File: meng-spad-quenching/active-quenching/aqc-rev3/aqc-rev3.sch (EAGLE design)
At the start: 274 parts, among them IC1 TPS7A4901, IC10 TPS7A3001, IC11 LT1534-1, IC12 74AHC1G04DCK, IC13 TLV271DBV, IC14 NC7WZ16P6X, IC15 LTC1711, IC16 HFA3134, IC17 HFA3135, IC18 USBLC6-2SC6Y, IC19 HFA3135, IC2 TPS7A4901, IC20 HFA3134, IC21 STM32F411RE, IC22 MAX572X, IC23 HFA3134, IC24 LM1117, IC25 HFA3134, IC26 THAT320, IC27 74AHC1G14DCK, IC28 NL17SZ125, IC29 TLV272DGK, IC3 LT1534-1, IC30 74AHC1G32DCK, IC31 74AHC1G08DCK, IC4 TLV272DGK, IC5 ADCMP582, IC6 DS1100LU-20+, IC7 HFA3134, IC8 NC7SV74K8X, IC9 HFA3134, M2 BSS806N, M3 BSS806N, Q6 IRLML6402TRPBF, SW1 MCU_RST, T1 MMBTH10, U1 MCP4725, U2 SN65EPT22DGK, U3 SN65EPT21DGK, X1 CONN_PULLDN_SENSE, X2 CONN_FORCE_QUENCH, X3 KEYSTONE-7774, X4 CONN_SPAD, X5 CONN_PHOTON_COUNTER, X6 KEYSTONE-7774, X7 CONN_SMU, X8 PN61729-S

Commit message: Fixed one-shot error, layout done
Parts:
- removed D7, D8: BAS40, diode:BAS40
- removed D9: (no value), diode:DIODE-SOD523
- removed L11: MI0805J102R-10, meng:INDUCTOR0805
- removed M3: BSS806N, meng:BSS806N
- removed Q6: IRLML6402TRPBF, microbuilder:MOSFET-PWIDE
- removed R77: 22R, resistor:R-EU_R0402
- removed R78: 0R, rcl-modified-footprints:R-EU_R0603
- removed R79: DNP, rcl-modified-footprints:R-EU_R0603
- removed R80: SOT-DIV23LF-03-1001-1001-BB, meng:DIVIDER_SOT23-5
- removed R82: 0R, rcl:R-EU_R0603
- removed R83, R84: 100R, rcl:R-EU_R0603
- removed R85: 470R, resistor:R-EU_R0603
- added C102: 4u7, rcl:C-EUC0603
- added C112, C90: 100n, rcl:C-EUC0603
- added C87: 100n, rcl-modified-footprints:C-EUC0603
- added C88, C89: 100n, rcl-modified-footprints:C-EUC0402
- added D2: CDBA140SL-HF, diode:DIODE-DO214AC
- added D3: TVS, diode:DIODE-SOD523
- added D5: BAS40, diode:BAS40
- added DNP1000: RLE_LOGO, meng:RLE_LOGO
- added IC32: LM1117, meng:LM1117
- added L8: MI0805J102R-10, meng:INDUCTOR0805
- added M1: BSS806N, meng:BSS806N
- added Q1: IRLML6402TRPBF, microbuilder:MOSFET-PWIDE
- added R47, R51: 0R, rcl-modified-footprints:R-EU_R0603
- added R50: 110R, 1%, rcl-modified-footprints:R-EU_R0603
- added R57: 100k, rcl-modified-footprints:R-EU_R0603
- added R60: 470R, resistor:R-EU_R0603
- added R61: 220k, rcl-modified-footprints:R-EU_R0603
- added R62: 100k, resistor:R-EU_R0603
- added R68: SOT-DIV23LF-03-1001-1001-BB, meng:DIVIDER_SOT23-5
- added R69: DNP, rcl-modified-footprints:R-EU_R0603
- added R70: 22R, resistor:R-EU_R0402
- C100: value 100n -> 47p; device rcl-modified-footprints:C-EUC0603 -> rcl:C-EUC0402
- C101, C23, C28, C36, C42, C45, C7, C76, C78: value 10n -> 100n
- C103, C108, C40, C98: device rcl:C-EUC0603 -> rcl-modified-footprints:C-EUC0603
- C104, C21, C27, C29, C43, C5, C80, C83: value 100n -> 10n
- C105, C99: value 4u7 -> 100n
- C107: value 100n -> 4u7; device rcl-modified-footprints:C-EUC0603 -> rcl:C-EUC0603
- C11: value 100n -> 10u; device rcl-modified-footprints:C-EUC0603 -> rcl:C-EUC0805
- C13: value 10u -> 47u, 20V; device rcl:C-EUC0805 -> rcl:CPOL-EUCT7343
- C15: value 47u, 20V -> 4u7; device rcl:CPOL-EUCT7343 -> rcl:C-EUC0805
- C16: value 4u7 -> 100n; device rcl:C-EUC0805 -> rcl-modified-footprints:C-EUC0603
- C17: value 4u7 -> 100n; device rcl-modified-footprints:C-EUC0603 -> rcl:C-EUC0603
- C18: value 100n -> 15n; device rcl-modified-footprints:C-EUC0603 -> rcl:C-EUC0603
- C19: value 10n -> 220p; device rcl-modified-footprints:C-EUC0402 -> rcl:C-EUC0603
- C20: value 10n -> 100n; device rcl-modified-footprints:C-EUC0402 -> rcl-modified-footprints:C-EUC0603
- C22: value 10n -> 4u7; device rcl-modified-footprints:C-EUC0402 -> rcl-modified-footprints:C-EUC0603
- C24, C84: value 100n -> 10n; device rcl:C-EUC0603 -> rcl-modified-footprints:C-EUC0402
- C25: value 15n -> 47u, 20V; device rcl:C-EUC0603 -> rcl:CPOL-EUCT7343
- C26: value 220p -> 47u, 20V; device rcl:C-EUC0603 -> rcl:CPOL-EUCT7343
- C30: value 47u, 20V -> 10n; device rcl:CPOL-EUCT7343 -> rcl:C-EUC0603
- C31: value 47u, 20V -> 1300p; device rcl:CPOL-EUCT7343 -> rcl:C-EUC0603
- C38: value 100n -> 10u; device rcl-modified-footprints:C-EUC0402 -> rcl:C-EUC0805
- C41: value 1300p -> 68u, 16V; device rcl:C-EUC0603 -> rcl:CPOL-EUCT7343
- C44: value 10u -> 4u7
- C46: value 68u, 16V -> 10n; device rcl:CPOL-EUCT7343 -> rcl-modified-footprints:C-EUC0402
- C50: value 100n -> 100p
- C51: device rcl:C-EUC0402 -> rcl-modified-footprints:C-EUC0603
- C53: value 4u7 -> 10n; device rcl:C-EUC0805 -> rcl-modified-footprints:C-EUC0603
- C54, C62, C77: device rcl:C-EUC0402 -> rcl-modified-footprints:C-EUC0402
- C55: value 10n -> 10u, 10V; device rcl:C-EUC0402 -> rcl:C-EUC0805
- C56: value 100p -> 4u7; device rcl-modified-footprints:C-EUC0402 -> rcl:C-EUC0805
- C57: value 10n -> 100n; device rcl-modified-footprints:C-EUC0603 -> rcl-modified-footprints:C-EUC0402
- C58, C92: device rcl-modified-footprints:C-EUC0603 -> rcl-modified-footprints:C-EUC0402
- C59: device rcl-modified-footprints:C-EUC0603 -> rcl:C-EUC0402
- C60: value 10u, 10V -> 100n; device rcl:C-EUC0805 -> rcl:C-EUC0402
- C61: value 4u7 -> 10n; device rcl:C-EUC0805 -> rcl-modified-footprints:C-EUC0402
- C63: value 100n -> 10n; device rcl:C-EUC0402 -> rcl-modified-footprints:C-EUC0402
- C65, C73: value 100n -> 10n; device rcl-modified-footprints:C-EUC0402 -> rcl:C-EUC0402
- C66: value 100p -> 100n; device rcl-modified-footprints:C-EUC0603 -> rcl:C-EUC0603
- C67: value 100n -> 33n
- C68: value 33n -> DNP
- C69: value DNP -> 100p; device rcl:C-EUC0603 -> rcl-modified-footprints:C-EUC0603
- C71: value 100n -> DNP; device rcl-modified-footprints:C-EUC0603 -> rcl-modified-footprints:C-EUC0402
- C72: value 10n -> 100n; device rcl-modified-footprints:C-EUC0603 -> rcl:C-EUC0402
- C74, C75: device rcl-modified-footprints:C-EUC0402 -> rcl-modified-footprints:C-EUC0603
- C79: value 4u7 -> 100n; device rcl:C-EUC0603 -> rcl-modified-footprints:C-EUC0402
- C81: value 4u7 -> 10n
- C82: device rcl:C-EUC0603 -> rcl:C-EUC0402
- C85: value 100n -> 4u7
- C86: value 100n -> 4u7; device rcl:C-EUC0402 -> rcl:C-EUC0603
- C91: device rcl-modified-footprints:C-EUC0603 -> rcl:C-EUC0603
- C93: value 10n -> 100n; device rcl:C-EUC0402 -> rcl-modified-footprints:C-EUC0603
- C94: value 47p -> 100n
- C96: value 100n -> 10n; device rcl-modified-footprints:C-EUC0603 -> rcl:C-EUC0402
- D4: value CDBA140SL-HF -> BAS40; device diode:DIODE-DO214AC -> diode:BAS40
- IC10: value TPS7A3001 -> LT1534-1; device Kramnik's Library:TPS7A -> meng:LT1534
- IC11: value LT1534-1 -> HFA3134; device meng:LT1534 -> meng:HFA3134
- IC12: value 74AHC1G04DCK -> HFA3134; device 74xx-little-de:74AHC1G04DCK -> meng:HFA3134
- IC13: value TLV271DBV -> HFA3134; device meng:TLV271DBV -> meng:HFA3134
- IC14: value NC7WZ16P6X -> LTC1711; device meng:NC7WZ16P6X -> meng:LTC1711
- IC15: value LTC1711 -> NC7SV74K8X; device meng:LTC1711 -> meng:NC7SV74K8X
- IC16: value HFA3134 -> 74AHC1G14DCK; device meng:HFA3134 -> 74xx-little-de:74AHC1G14DCK
- IC17: value HFA3135 -> NL17SZ125; device meng:HFA3135 -> 74xx-little-de:74AHC1G125DCK
- IC18: value USBLC6-2SC6Y -> 74AHC1G04DCK; device meng:USBLC6 -> 74xx-little-de:74AHC1G04DCK
- IC19: value HFA3135 -> 74AHC1G32DCK; device meng:HFA3135 -> 74xx-little-de:74AHC1G32DCK
- IC20: value HFA3134 -> NC7WZ16P6X; device meng:HFA3134 -> meng:NC7WZ16P6X
- IC21: value STM32F411RE -> 74AHC1G08DCK; device meng:STM32F405RG -> 74xx-little-de:74AHC1G08DCK
- IC22: value MAX572X -> 74AHC1G08DCK; device meng:MAX572X -> 74xx-little-de:74AHC1G08DCK
- IC24: value LM1117 -> TLV272DGK; device meng:LM1117 -> meng:TLV272DGK
- IC25: value HFA3134 -> THAT320; device meng:HFA3134 -> meng:THAT320
- IC26: value THAT320 -> TLV272DGK; device meng:THAT320 -> meng:TLV272DGK
- IC27: value 74AHC1G14DCK -> HFA3134; device 74xx-little-de:74AHC1G14DCK -> meng:HFA3134
- IC28: value NL17SZ125 -> TLV271DBV; device 74xx-little-de:74AHC1G125DCK -> meng:TLV271DBV
- IC29: value TLV272DGK -> USBLC6-2SC6Y; device meng:TLV272DGK -> meng:USBLC6
- IC30: value 74AHC1G32DCK -> STM32F411RE; device 74xx-little-de:74AHC1G32DCK -> meng:STM32F405RG
- IC31: value 74AHC1G08DCK -> MAX572X; device 74xx-little-de:74AHC1G08DCK -> meng:MAX572X
- IC4: value TLV272DGK -> ADCMP582; device meng:TLV272DGK -> meng:ADCMP582
- IC5: value ADCMP582 -> HFA3134; device meng:ADCMP582 -> meng:HFA3134
- IC6: value DS1100LU-20+ -> HFA3135; device meng:DS1100L -> meng:HFA3135
- IC7: value HFA3134 -> DS1100LU-20+; device meng:HFA3134 -> meng:DS1100L
- IC8: value NC7SV74K8X -> HFA3135; device meng:NC7SV74K8X -> meng:HFA3135
- IC9: value HFA3134 -> TPS7A3001; device meng:HFA3134 -> Kramnik's Library:TPS7A
- L10: value PE-0603FB601ST -> MI0805J102R-10; device meng:INDUCTOR0603 -> meng:INDUCTOR0805
- L2: value PE-0603FB601ST -> 732-1699-2-ND; device meng:INDUCTOR0603 -> meng:WE_INDUCTOR
- L4: value 732-1699-2-ND -> PE-0603FB601ST; device meng:WE_INDUCTOR -> meng:INDUCTOR0603
- L9: value MI0805J102R-10 -> PE-0603FB601ST; device meng:INDUCTOR0805 -> meng:INDUCTOR0603
- R10: value 2k2 -> 76k8
- R11: value 2k2 -> 137k
- R12: value 76k8 -> 2k2
- R13: value 137k -> 2k2
- R14: device rcl-modified-footprints:R-EU_R0603 -> resistor:R-EU_R0603
- R15: value DNP -> 1k; device rcl-modified-footprints:R-EU_R0603 -> resistor:R-EU_R0603
- R16: value 49R9 -> 6k8; device rcl-modified-footprints:R-EU_R0402 -> resistor:R-EU_R0603
- R18: value DNP -> 1k
- R20: value DNP -> 49R9; device rcl-modified-footprints:R-EU_R0603 -> rcl-modified-footprints:R-EU_R0402
- R22: value 1k -> 150R; device resistor:R-EU_R0603 -> rcl-modified-footprints:R-EU_R0402
- R23: value 1k -> 220R, 1%; device resistor:R-EU_R0603 -> rcl-modified-footprints:R-EU_R0603
- R24: value 6k8 -> DNP; device resistor:R-EU_R0603 -> rcl-modified-footprints:R-EU_R0603
- R25: value 150R -> DNP; device rcl-modified-footprints:R-EU_R0402 -> rcl-modified-footprints:R-EU_R0603
- R26: value 220R -> DNP
- R27, R28: value 220k -> DNP
- R29: value 150R -> 100R; device rcl-modified-footprints:R-EU_R0402 -> resistor:R-EU_R0603
- R3, R74: value DNP -> 0R
- R30: value 100R -> 16k9; device rcl-modified-footprints:R-EU_R0402 -> rcl:R-EU_R0603
- R31: value 10k -> 150R; device rcl-modified-footprints:R-EU_R0603 -> rcl-modified-footprints:R-EU_R0402
- R32: value 220R -> 76k8
- R33: value 100k -> 100R; device rcl-modified-footprints:R-EU_R0603 -> rcl-modified-footprints:R-EU_R0402
- R34: value 100R -> 24k; device resistor:R-EU_R0603 -> rcl-modified-footprints:R-EU_R0603
- R35: value 16k9 -> 49R9; device rcl:R-EU_R0603 -> rcl-modified-footprints:R-EU_R0402
- R36: value 100k -> 10k
- R37, R42: value DNP -> 100R, 1%
- R38: value 76k8 -> 200R, 1%
- R39: value 10k -> 200R, 1%
- R4: value 0R -> DNP
- R40: value 24k -> 49R9
- R41: value 49R9 -> 1k4; device rcl-modified-footprints:R-EU_R0402 -> resistor:R-EU_R0603
- R43: value 220R -> 1k; device rcl-modified-footprints:R-EU_R0603 -> resistor:R-EU_R0603
- R44: value 49R9 -> 1k; device rcl-modified-footprints:R-EU_R0603 -> resistor:R-EU_R0603
- R45: value 0R -> 2k; device rcl-modified-footprints:R-EU_R0603 -> rcl:R-EU_R0603
- R46: value 100R -> 220R, 1%
- R48: value 1k4 -> 1k
- R49: value 100R -> 49R9; device rcl-modified-footprints:R-EU_R0603 -> rcl:R-EU_R0603
- R5: value DNP -> 29k4
- R52: value 1k -> 49R9; device resistor:R-EU_R0603 -> rcl:R-EU_R0603
- R53: value 1k -> 220k; device resistor:R-EU_R0603 -> rcl-modified-footprints:R-EU_R0603
- R54: value 2k -> 10k; device rcl:R-EU_R0603 -> rcl-modified-footprints:R-EU_R0603
- R55: value 1k -> 470R
- R56: value 220R -> 100k
- R58: value 49R9 -> 4k7; device rcl:R-EU_R0603 -> resistor:R-EU_R0603
- R59: value 220R -> 127k, 1%
- R6: value 29k4 -> 2k49
- R63: value 49R9 -> 274R, 1%; device rcl:R-EU_R0603 -> rcl-modified-footprints:R-EU_R0603
- R64: value 220k -> 102k, 1%
- R65: value 220R -> 470R; device rcl-modified-footprints:R-EU_R0603 -> resistor:R-EU_R0603
- R66: value 4k7 -> DNP; device resistor:R-EU_R0603 -> rcl-modified-footprints:R-EU_R0603
- R67: value 100k -> 22R; device resistor:R-EU_R0603 -> resistor:R-EU_R0402
- R7: value 2k49 -> 10R; device rcl-modified-footprints:R-EU_R0603 -> resistor:R-EU_R0603
- R71: value 470R -> 0R; device resistor:R-EU_R0603 -> rcl-modified-footprints:R-EU_R0603
- R72: value 470R -> DNP; device resistor:R-EU_R0603 -> rcl-modified-footprints:R-EU_R0603
- R73: value 220k -> 0R; device rcl-modified-footprints:R-EU_R0603 -> rcl:R-EU_R0603
- R75: value DNP -> 100R; device rcl-modified-footprints:R-EU_R0603 -> rcl:R-EU_R0603
- R76: value 22R -> 100R; device resistor:R-EU_R0402 -> rcl:R-EU_R0603
- R8: value 10R -> 16k9
- R9: value 16k9 -> DNP; device resistor:R-EU_R0603 -> rcl-modified-footprints:R-EU_R0603
- TP1: value GND -> TPTP15R; device Kramnik's Library:KEYSTONE_5000 -> testpad:TPTP15R
- TP10: value TP_VSCOPE -> TPB1,27; device meng:TP-SCOPE_H -> testpad:TPB1,27
- TP11: value TPTP06R -> TPTP15R; device testpad:TPTP06R -> testpad:TPTP15R
- TP12: value TPB1,27 -> TPTP06R; device testpad:TPB1,27 -> testpad:TPTP06R
- TP2, TP8: value TPTP15R -> TPB1,27; device testpad:TPTP15R -> testpad:TPB1,27
- TP3: value TPB1,27 -> TPTP15R; device testpad:TPB1,27 -> testpad:TPTP15R
- TP5: value TPTP15R -> GND; device testpad:TPTP15R -> Kramnik's Library:KEYSTONE_5000
- TP9: value TPB1,27 -> TP_VSCOPE; device testpad:TPB1,27 -> meng:TP-SCOPE_H
- renumbered R81 to R64
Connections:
- new net CAP_!RESET: IC17A.OE, IC22A.O
- new net N$11: C71.2, IC14.-IN, R51.1
- new net N$13: C71.1, IC14.+IN, R47.1
- net !FORCE_QUENCH: now also IC15.!PRE, IC18A.O, IC22A.I0; no longer IC12A.O, IC8.!PRE
- net !LOGIC_QUENCH: now also IC13_Q1.B, IC15.!Q, IC16A.I, TP12.TP; no longer IC20_Q1.B, IC27A.I, IC8.!Q, TP11.TP
- net !MCU_SHDN_BOOST: now also IC30.PA2/UART2_TX; no longer IC21.PA2/UART2_TX
- net !MCU_SHDN_CUK: now also IC10.!SHDN, IC30.PA1; no longer IC11.!SHDN, IC21.PA1
- net !MCU_SMPS_PRECHG: now also IC30.PA3/UART2_RX, R58.2; no longer IC21.PA3/UART2_RX, R66.2
- net !ONE_SHOT_CLR: now also IC14.Q, IC21A.I1; no longer IC15.!Q, IC31A.I1
- net BLANKING_LATCH_EN: now also R24.1, R25.1, R26.1, R27.1, R28.1; no longer R17.1, R18.1, R19.1, R20.1, R21.1
- net BOOST_STAGE1: now also C13.+, R4.1, R9.1; no longer C15.+, R3.1, R5.1
- net BOOST_SW_NODE: now also L2.P$2, R7.1; no longer L4.P$2, R8.1
- net CCS_STEERING_TAIL: now also IC13_Q1.E, IC13_Q2.E, IC23_Q1.C; no longer IC20_Q1.E, IC20_Q2.E, IC25_Q1.C
- net CCS_VA_SETPOINT: now also IC11_Q2.E, IC23_Q2.C; no longer IC23_Q2.E, IC25_Q2.C
- net COMP_HYS: now also IC4.HYS, R36.2; no longer IC5.HYS, R39.2
- net COMP_LE_N: now also IC4.!LE; no longer IC5.!LE
- net COMP_LE_P: now also IC4.LE; no longer IC5.LE
- net COMP_Q_N: now also IC4.!Q, R22.1, R33.1; no longer IC5.!Q, R25.1, R30.1
- net COMP_Q_P: now also IC4.Q, R31.1, R33.2; no longer IC5.Q, R29.1, R30.2
- net COMP_VTN: now also IC4.VTN, R21.2; no longer IC5.VTN, R15.2
- net COMP_VTT: now also IC4.VTT, R20.1; no longer IC5.VTT, R16.1
- net DAC1_!CLR: now also IC30.PD2/SDIO_CMD, IC31.!CLR; no longer IC21.PD2/SDIO_CMD, IC22.!CLR
- net DAC1_DIN: now also IC30.PC12/SDIO_CLK, IC31.DIN; no longer IC21.PC12/SDIO_CLK, IC22.DIN
- net DAC1_DOUT: now also IC30.PC11/SDIO_D3, IC31.DOUT; no longer IC21.PC11/SDIO_D3, IC22.DOUT
- net DAC1_SCLK: now also IC30.PC10/SDIO_D2, IC31.SCLK; no longer IC21.PC10/SDIO_D2, IC22.SCLK
- net DAC2_ADDRSEL: now also IC30.PB5; no longer IC21.PB5
- net DAC2_SCL: now also IC30.PB6/I2C1_SCL, R12.2; no longer IC21.PB6/I2C1_SCL, R11.2
- net DAC2_SDA: now also IC30.PB7/I2C1_SDA, R13.2; no longer IC21.PB7/I2C1_SDA, R10.2
- net DELTAV_BASE: now also IC23_Q1.B, IC26_A.OUT; no longer IC25_Q1.B, IC4_A.OUT
- net DELTAV_FB: now also IC23_Q1.E, R59.1, R63.2; no longer IC25_Q1.E, R65.2, R73.1
- net DELTAV_VGND: now also IC26_A.-IN, R59.2; no longer IC4_A.-IN, R73.2
- net DFLOP_!CLR: now also IC15.!CLR, IC21A.O; no longer IC31A.O, IC8.!CLR
- net DIAMOND_BASE: now also IC27_Q1.B, IC27_Q2.B, IC28.OUT; no longer IC13.OUT, IC7_Q1.B, IC7_Q2.B
- net DIAMOND_FB: now also IC27_Q1.E, IC28.-IN, R68.TOP; no longer IC13.-IN, IC7_Q1.E, R80.TOP
- net DIAMOND_FB_R: now also IC27_Q2.E, R68.BOTTOM; no longer IC7_Q2.E, R80.BOTTOM
- net DIAMOND_IBIAS_BOTTOM: now also C51.2, IC5_Q2.C, IC8_Q2.B, R38.1; no longer C57.2, IC17_Q2.B, IC9_Q2.C, R43.1
- net DIAMOND_IBIAS_MID: now also IC25Q3.B, IC25Q4.B, IC25Q4.C, IC5_Q1.C; no longer IC26Q3.B, IC26Q4.B, IC26Q4.C, IC9_Q1.C
- net DIAMOND_IBIAS_TOP: now also C51.1, IC12_Q2.B, IC25Q3.C, R39.2; no longer C57.1, IC16_Q2.B, IC26Q3.C, R59.2
- net DIAMOND_IN: now also IC11_Q1.C, IC11_Q2.C, IC12_Q1.B, IC8_Q1.B, R46.1; no longer IC16_Q1.B, IC17_Q1.B, IC23_Q1.C, IC23_Q2.C, R56.1
- net DMD_IN_CASC: now also IC6_Q1.E, IC8_Q1.C; no longer IC17_Q1.C, IC19_Q1.E
- net DMD_IN_NPN_E: now also IC12_Q1.E, R38.2; no longer IC16_Q1.E, R43.2
- net DMD_IN_PNP_E: now also IC8_Q1.E, R39.1; no longer IC17_Q1.E, R59.1
- net DMD_OP_CASC: now also IC6_Q2.E, IC8_Q2.C; no longer IC17_Q2.C, IC19_Q2.E
- net DMD_OP_NPN: now also C50.1, IC12_Q2.E, R42.2; no longer C56.1, IC16_Q2.E, R49.2
- net DMD_OP_PNP: now also C50.2, IC8_Q2.E, R37.1; no longer C56.2, IC17_Q2.E, R46.1
- net DMD_OUT: now also R35.1, R37.2, R42.1; no longer R41.1, R46.2, R49.1
- net FORCE_QUENCH: now also IC18A.I, IC19A.O; no longer IC12A.I, IC30A.O
- net FORCE_QUENCH_USER: now also IC19A.I0, R49.2; no longer IC30A.I0, R58.2
- net GND: now also C102.2, C112.2, C13.-, C15.2, C25.-, C26.-, C30.2, C31.2, C45.2, C46.2, C56.2, C57.2, C7.2, C82.2, C87.2, C88.2, C89.2, C90.2, D2.C, D3.A, IC14.LEN, IC16P.GND, IC17P.GND, IC18P.GND, IC19P.GND, IC20.GND, IC21P.GND, IC22P.GND, IC24_A.+IN, IC25SUBC.SUBC, IC26_A.+IN, IC28.V-, IC29.GND, IC30.VSS1, IC30.VSS2, IC30.VSSA, IC31.CSB, IC31.GND, IC31.M/!Z, IC32.GND, IC4.GND, IC6_Q1.C, IC7.GND, IC9.GND, L10.P$2, M1.S, R14.2, R15.2, R19.1, R20.2, R21.1, R30.1, R31.2, R34.2, R43.2, R44.2, R48.2, R49.1, R50.1, R6.2, R68.MIDDLE, R71.2, R72.2, R74.2, R8.1, TP4.TP, TP5.P$1, TP9.GND; no longer C13.2, C15.-, C25.2, C26.2, C30.-, C31.-, C40.2, C41.2, C5.2, C50.2, C51.2, C71.2, C78.2, D4.C, D9.A, IC11.GND, IC12P.GND, IC13.V-, IC15.LEN, IC18.GND, IC19_Q1.C, IC21.VSS1, IC21.VSS2, IC21.VSSA, IC22.CSB, IC22.GND, IC22.M/!Z, IC24.GND, IC26SUBC.SUBC, IC27P.GND, IC28P.GND, IC29_A.+IN, IC30P.GND, IC31P.GND, IC4_A.+IN, IC5.GND, IC6.GND, IC8.GND, L11.P$2, M3.S, R15.1, R16.2, R23.2, R25.2, R26.1, R29.2, R35.1, R37.1, R40.2, R45.2, R52.2, R53.2, R55.2, R58.1, R7.2, R78.2, R79.2, R80.MIDDLE, R9.1, TP1.P$1, TP10.GND, TP5.TP
- net HOLDOFF_TRIG: now also IC15.CLK; no longer IC8.CLK
- net LDO_N10V0_FB_CH1: now also C40.2, IC9.FB, R32.1, R34.1; no longer C45.2, IC10.FB, R38.1, R40.1
- net LDO_N10V0_NR_SS_CH1: now also C53.1, IC9.NR/SS; no longer C59.1, IC10.NR/SS
- net LDO_P10V0_FB_CH1: now also C6.2, R11.1; no longer C7.2, R13.1
- net LDO_P5V0_FB_CH1: now also C5.2, R10.1; no longer C6.2, R12.1
- net LOGIC_QUENCH: now also IC13_Q2.B, IC15.Q; no longer IC20_Q2.B, IC8.Q
- net LOGIC_QUENCH_BUF: now also IC16A.O, IC20.IN1, IC20.IN2, IC22A.I1, IC7.IN, R40.2; no longer IC14.IN1, IC14.IN2, IC27A.O, IC28A.OE, IC6.IN, R44.2
- net MCU_AQC_RLY: now also IC30.PB13/I2S2_CK, R76.2; no longer IC21.PB13/I2S2_CK, R84.2
- net MCU_BOOT0: now also IC30.BOOT0, R69.2, R71.1; no longer IC21.BOOT0, R74.2, R78.1
- net MCU_BOOT1: now also IC30.PB2-BOOT1, R66.2, R72.1; no longer IC21.PB2-BOOT1, R75.2, R79.1
- net MCU_IVTEST_RLY: now also IC30.PB12/I2S2_WS, R75.2; no longer IC21.PB12/I2S2_WS, R83.2
- net MCU_JTCK: now also IC30.PA14/JTCK; no longer IC21.PA14/JTCK
- net MCU_JTDO: now also IC30.PB3/JTDO; no longer IC21.PB3/JTDO
- net MCU_JTMS: now also IC30.PA13/JTMS; no longer IC21.PA13/JTMS
- net MCU_LED1: now also IC30.PC0, R65.2; no longer IC21.PC0, R72.2
- net MCU_LED2: now also IC30.PC1, R60.2; no longer IC21.PC1, R71.2
- net MCU_LED3: now also IC30.PC2, R55.2; no longer IC21.PC2, R85.2
- net MCU_NRST: now also C81.1, IC30.NRST; no longer C78.1, IC21.NRST
- net MCU_OSC_IN: now also IC30.PH0/OSC_IN; no longer IC21.PH0/OSC_IN
- net MCU_OSC_OUT: now also IC30.PH1/OSC_OUT; no longer IC21.PH1/OSC_OUT
- net MCU_PB11: now also C103.1, IC30.PB11; no longer C100.1, IC21.PB11
- net MCU_TIM2_CH1_IN: now also IC30.PA0, R40.1; no longer IC21.PA0, R44.1
- net MCU_TIM2_CH1_OUT_1: now also IC21A.I0, IC30.PA5/SPI1_SCK; no longer IC21.PA5/SPI1_SCK, IC31A.I0
- net MCU_TIM2_CH1_OUT_2: now also IC19A.I1, IC30.PA15/JTDI; no longer IC21.PA15/JTDI, IC30A.I1
- net MCU_USB_FS_D_N: now also C100.1, IC30.PA11, R70.1; no longer C97.1, IC21.PA11, R77.1
- net MCU_USB_FS_D_P: now also C97.1, IC30.PA12, R67.1; no longer C94.1, IC21.PA12, R76.1
- net MCU_VCAP_1: now also IC30.VCAP_1, R74.1; no longer IC21.VCAP_1, R45.1
- net MCU_VCAP_2: now also C111.1, IC30.VCAP_2; no longer C109.1, IC21.VCAP_2
- net N$1: now also R18.2; no longer R14.2
- net N$10: now also IC24_B.-IN, R56.1, R57.2; no longer IC29_B.-IN, R33.2, R36.1
- net N$12: now also C78.1, Q1.G, R58.1, R62.1; no longer C82.1, Q6.G, R66.1, R67.1
- net N$15: now also M1.G, R75.1; no longer M2.G, R83.1
- net N$16: now also IC27_Q1.C, IC5_Q1.E; no longer IC7_Q1.C, IC9_Q1.E
- net N$18: now also R5.1; no longer R7.1
- net N$20: now also IC10.PGND; no longer IC11.PGND
- net N$24: now also R60.1; no longer R71.1
- net N$26: now also IC27_Q2.C, IC5_Q2.E; no longer IC7_Q2.C, IC9_Q2.E
- net N$29: now also IC20.OUT1, IC20.OUT2, R52.2; no longer IC14.OUT1, IC14.OUT2, R63.2
- net N$3: now also M2.G, R76.1; no longer M3.G, R84.1
- net N$31: now also R55.1; no longer R85.1
- net N$4: now also D5.A, M2.D; no longer D8.A, M3.D
- net N$5: now also IC24_A.OUT; no longer IC29_A.OUT
- net N$51: now also R15.1; no longer R23.1
- net N$52: now also R14.1; no longer R22.1
- net N$54: now also R7.2; no longer R8.2
- net N$55: now also C18.1, R16.1; no longer C25.1, R24.1
- net N$56: now also C19.1, R16.2; no longer C26.1, R24.2
- net N$57: now also R8.2; no longer R9.2
- net N$6: now also D4.A, M1.D; no longer D7.A, M2.D
- net N$60: now also IC10.RCSL, R44.1; no longer IC11.RCSL, R53.1
- net N$61: now also IC10.RVSL, R43.1; no longer IC11.RVSL, R52.1
- net N$62: now also C30.1, R29.2; no longer C40.1, R34.2
- net N$63: now also C67.1, R45.1; no longer C68.1, R54.1
- net N$64: now also C68.1, IC10.VC, R45.2; no longer C69.1, IC11.VC, R54.2
- net N$65: now also IC10.RT, R30.2; no longer IC11.RT, R35.2
- net N$67: now also IC10.NFB, R41.2, R48.1; no longer IC11.NFB, R48.2, R55.1
- net N$68: now also C41.+, IC10.COL, R29.1; no longer C46.+, IC11.COL, R34.1
- net N$69: now also C41.-, D2.A; no longer C46.-, D4.A
- net N$7: now also IC24_B.OUT, R51.2, R57.1; no longer IC15.-IN, IC29_B.OUT, R33.1
- net N$73: now also R3.2; no longer R6.2
- net N$8: now also C31.1, IC10.CT; no longer C41.1, IC11.CT
- net N$88: now also IC25Q1.B, IC25Q1.C, IC25Q2.B, IC25Q4.E; no longer IC26Q1.B, IC26Q1.C, IC26Q2.B, IC26Q4.E
- net N$89: now also IC25Q2.C, IC25Q3.E; no longer IC26Q2.C, IC26Q3.E
- net N$9: now also R65.1; no longer R72.1
- net N$92: now also IC31.REF, R73.2; no longer IC22.REF, R82.2
- net NC_DAC1_IRQ: now also IC31.!IRQ; no longer IC22.!IRQ
- net NC_ONE_SHOT_CLR: now also IC14.!Q; no longer IC15.Q
- net ONE_SHOT_CAP: now also C69.1, IC17A.O, R47.2; no longer C66.1, IC15.+IN, IC28A.O
- net ONE_SHOT_FB: now also R53.1, R54.1; no longer R27.1, R31.1
- net ONE_SHOT_VGND: now also IC24_A.-IN, R53.2, R61.1; no longer IC29_A.-IN, R27.2, R28.1
- net PHOTON_COUNT_OUT: now also R52.1; no longer R63.1
- net PP_N5V0_ANALOG: now also C36.1, C37.1, C40.1, C54.1, C61.1, C79.1, C93.1, IC14.V-, IC24_A.V-, IC26_A.V-, IC4.VEE, IC9.OUT, R32.2, R36.1, R54.2, R63.1, TP11.TP; no longer C28.1, C29.1, C39.1, C44.1, C52.1, C73.1, C95.1, IC10.OUT, IC15.V-, IC29_A.V-, IC4_A.V-, IC5.VEE, R31.2, R38.2, R39.1, R65.1, TP8.TP
- net PP_N6V0_CUK: now also C52.1, C55.1, IC9.EN, IC9.IN, R41.1; no longer C58.1, C60.1, IC10.EN, IC10.IN, R48.1
- net PP_P15V0_ANALOG: now also C11.1, C6.1, C74.1, C75.1, IC12_Q1.C, IC12_Q2.C, IC25Q1.E, IC25Q2.E, R11.2, R46.2, TP1.TP; no longer C13.1, C71.1, C72.1, C9.1, IC16_Q1.C, IC16_Q2.C, IC26Q1.E, IC26Q2.E, R13.2, R56.2, TP2.TP
- net PP_P16V0_BOOST: now also C25.+, C8.1, R3.1, R9.2; no longer C11.1, C30.+, R3.2, R4.1
- net PP_P3V3: now also C105.1, C109.1, C110.1, C16.1, C21.1, C43.1, C57.1, C58.1, C59.1, C60.1, C65.1, C72.1, C73.1, C82.1, C88.1, C89.1, C90.1, C94.1, C95.1, C96.1, C98.1, IC15.D, IC15.VDD, IC16P.VCC, IC17A.I, IC17P.VCC, IC18P.VCC, IC19P.VCC, IC20.VCC, IC21P.VCC, IC22P.VCC, IC29.VBUS, IC30.VBAT, IC30.VDD1, IC30.VDD2, IC30.VDD3, IC30.VDD4, IC31.!LDAC, IC31.VDDIO, IC32.OUT, IC32.TAB, IC4.VCCO, IC7.VCC, L4.P$1, R12.1, R13.1, R66.1, R69.1; no longer C103.1, C106.1, C107.1, C22.1, C32.1, C33.1, C35.1, C49.1, C5.1, C50.1, C51.1, C54.1, C55.1, C76.1, C77.1, C81.1, C91.1, C92.1, C93.1, IC12P.VCC, IC14.VCC, IC18.VBUS, IC21.VBAT, IC21.VDD1, IC21.VDD2, IC21.VDD3, IC21.VDD4, IC22.!LDAC, IC22.VDDIO, IC24.OUT, IC24.TAB, IC27P.VCC, IC28A.I, IC28P.VCC, IC30P.VCC, IC31P.VCC, IC5.VCCO, IC6.VCC, IC8.D, IC8.VDD, L2.P$1, R10.1, R11.1, R74.1, R75.1
- net PP_P3V3_AV_DET_DAC: now also C20.1, C22.1, L4.P$2, R17.2; no longer C17.1, C18.1, L2.P$2, R42.2
- net PP_P3V3_VDDA: now also C91.1, IC30.VDDA; no longer C79.1, IC21.VDDA
- net PP_P5V0_ANALOG: now also C24.1, C28.1, C29.1, C35.1, C39.1, C46.1, C49.1, C5.1, C76.1, C77.1, C87.1, C9.1, C92.1, C99.1, IC11_Q1.B, IC11_Q2.B, IC13_Q1.C, IC14.V+, IC24_A.V+, IC26_A.V+, IC28.V+, IC4.VCCI, IC5_Q1.B, IC5_Q2.B, IC6_Q1.B, IC6_Q2.B, L9.P$1, R10.2, R56.2, TP3.TP; no longer C111.1, C19.1, C20.1, C21.1, C37.1, C6.1, C65.1, C74.1, C75.1, C8.1, C96.1, IC13.V+, IC15.V+, IC19_Q1.B, IC19_Q2.B, IC20_Q1.C, IC23_Q1.B, IC23_Q2.B, IC29_A.V+, IC4_A.V+, IC5.VCCI, IC9_Q1.B, IC9_Q2.B, L10.P$1, R12.2, R36.2, TP4.TP
- net PP_P5V0_DAC1: now also C101.1, C102.1, IC31.VDD, L9.P$2, R73.1; no longer C98.1, C99.1, IC22.VDD, L10.P$2, R82.1
- net PULLDN_SENSE_R_CONN: now also R23.1; no longer R32.1
- net SMPS_USB_VDD: now also C112.1, C15.1, C17.1, C26.+, C44.1, C56.1, C66.1, C78.2, D4.C, D5.C, IC10.VIN, L2.P$1, Q1.D; no longer C110.1, C16.1, C24.1, C31.+, C53.1, C61.1, C67.1, C82.2, D7.C, D8.C, IC11.VIN, L4.P$1, Q6.D
- net SPAD_PULLDN_SENSE: now also IC4.VN, IC6_Q2.C, R23.2; no longer IC19_Q2.C, IC5.VN, R32.2
- net STEERING_CASC: now also IC11_Q1.E, IC13_Q2.C; no longer IC20_Q2.C, IC23_Q1.E
- net TAP1: now also IC7.TAP1, R28.2; no longer IC6.TAP1, R21.2
- net TAP2: now also IC7.TAP2, R24.2; no longer IC6.TAP2, R17.2
- net TAP3: now also IC7.TAP3, R26.2; no longer IC6.TAP3, R19.2
- net TAP4: now also IC7.TAP4, R25.2; no longer IC6.TAP4, R18.2
- net TAP5: now also IC7.TAP5, R27.2; no longer IC6.TAP5, R20.2
- net TP_FB_CUK: now also IC10.FB, TP10.TP; no longer IC11.FB, TP12.TP
- net TP_SYNC_BOOST: now also TP2.TP; no longer TP3.TP
- net TP_SYNC_CUK: now also IC10.SYNC, TP8.TP; no longer IC11.SYNC, TP9.TP
- net USBCONN_P1: now also C104.1, L8.P$1; no longer C101.1, L9.P$1
- net USBCONN_P4: now also L10.P$1; no longer L11.P$1
- net USBD_CONN_N: now also IC29.I/O2; no longer IC18.I/O2
- net USBD_CONN_P: now also IC29.I/O1_1; no longer IC18.I/O1_1
- net USBD_TVS_N: now also IC29.I/O2_2, R70.2; no longer IC18.I/O2_2, R77.2
- net USBD_TVS_P: now also IC29.I/O1_2, R67.2; no longer IC18.I/O1_2, R76.2
- net USB_VDD: now also C106.1, C107.1, IC32.IN, L8.P$2, Q1.S, R62.2; no longer C104.1, C105.1, IC24.IN, L9.P$2, Q6.S, R67.2
- net VA_BASE: now also IC23_Q2.B, IC26_B.OUT; no longer IC25_Q2.B, IC4_B.OUT
- net VA_FB: now also IC23_Q2.E, IC26_B.-IN, R50.2; no longer IC25_Q2.E, IC4_B.-IN, R26.2
- net VREF_AV_DET: now also C32.1, C33.1, IC4.VP, R17.1, R18.1, R19.2; no longer C36.1, C43.1, IC5.VP, R14.1, R37.2, R42.1
- net VREF_DELTAV_SETPOINT: now also IC31.OUT0; no longer IC22.OUT0
- net VREF_DIAMOND_IBIAS: now also IC28.+IN, IC31.OUT1; no longer IC13.+IN, IC22.OUT1
- net VREF_EXTRA_2: now also IC31.OUT5; no longer IC22.OUT5
- net VREF_EXTRA_3: now also IC31.OUT6; no longer IC22.OUT6
- net VREF_EXTRA_4: now also IC31.OUT7; no longer IC22.OUT7
- net VREF_ONE_SHOT_CCS: now also IC31.OUT4, R61.2; no longer IC22.OUT4, R28.2
- net VREF_ONE_SHOT_COMP: now also IC24_B.+IN, IC31.OUT2; no longer IC22.OUT2, IC29_B.+IN
- net VREF_VA_SETPOINT: now also IC26_B.+IN, IC31.OUT3; no longer IC22.OUT3, IC4_B.+IN
- net V_SCOPE: now also R35.2, TP9.1; no longer R41.2, TP10.1
- net V_SPAD: now also D3.C; no longer D9.C
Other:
- note added: ""R_L""
- note added: "- Redesigned level shifter circuit for faster speed and independent control of delta-V and VA"
- note added: "- Redesigned one-shot for lower jitter, and added option for digital one-shot using MCU"
- note added: "- Removed slew and delay generators, since we can trap ion and operate APDs as-is, or place a slowdown cap across load resistor of level shifter"
- note added: "- Switched boost inductor to be larger to prevent saturation and improve max. conversion ratio"
- note added: "- Switched to faster HFA3134/HFA3135 matched BJTs for output buffer, and added extra cascode stacks to prevent breakdown"
- note added: "- Switched upper biasing mirror to THAT320 BJTs due to excessive VGS requirement in ALD MOSFET arrays"
- note added: "1/2 * R_L"
- note added: "12"
- note added: "1V/V swing 0V = max swing 4V = no swing"
- note added: "2V/V offset"
- note added: "3.0"
- note added: "5/4 * R_L"
- note added: "Assert when +IN falls below -IN"
- note added: "DAC outputs between 0V and 4.096V Need to multiply by 5/4 to get full range of output currents."
- note added: "DIAMOND BIASING"
- note added: "Example Bias Point:"
- note added: "HIGH-SPEED USER IO GLUE LOGIC"
- note added: "Insufficient recovery blanking results in self re-triggering Pick lowest delay tap that compensates a given coax cable In the future, this process can be automated with a digitally-tunable delay based on an ECL counter circuit."
- note added: "LEVEL SHIFTER BIASING"
- note added: "LINEAR ACTIVE QUENCHING CIRCUIT FOR CMOS SPADS"
- note added: "Net Class: 100OHM_DIFF"
- note added: "Optional noise filter"
- note added: "Pulling either input low will reset timing capacitor. This gate is necessary to prevent !PRE! and !CLR! from being asserted simultaneously. When !PRE! is asserted, !CLR! is forced to be de-asserted."
- note added: "THAT Transistor Array Part Selection Note: Default Beta > 60 Pick "A" variant for Beta > 150 Pick "B" bariant for Beta > 300"
- note added: "To output buffer"
- note added: "USB Inrush Limiting: See pg. 7 of FTDI App. Note 146"
- note added: "f_T peaks at 10.5mA collector current f_T > 5GHz between ~2mA and ~12mA (and is higher for greater V_CE)"
- note removed: "- Removed slew and delay generators, since we can trap ion and operate APDs as-in"
- note removed: "- Switched biasing mirrors to THAT300/320 BJTs due to excessive VGS requirement in ALD MOSFET arrays"
- note removed: "- Switched boost inductor to be larger to prevent saturation"
- note removed: "1V/V offset"
- note removed: "2.0"
- note removed: "Insufficient recovery blanking results in self re-triggering Pick lowest delay tap that compensates a given coax cable"
- note removed: "LINEAR ACTIVE SPAD QUENCHING CIRCUIT"
- note removed: "Transistor Array Part Selection Note: Default Beta > 60 Pick "A" variant for Beta > 150 Pick "B" bariant for Beta > 300"
- note removed: "USB Inrush Limiting: See pg. 7 of FTDI AN_146"
- note removed: "Zdiff = 100R"

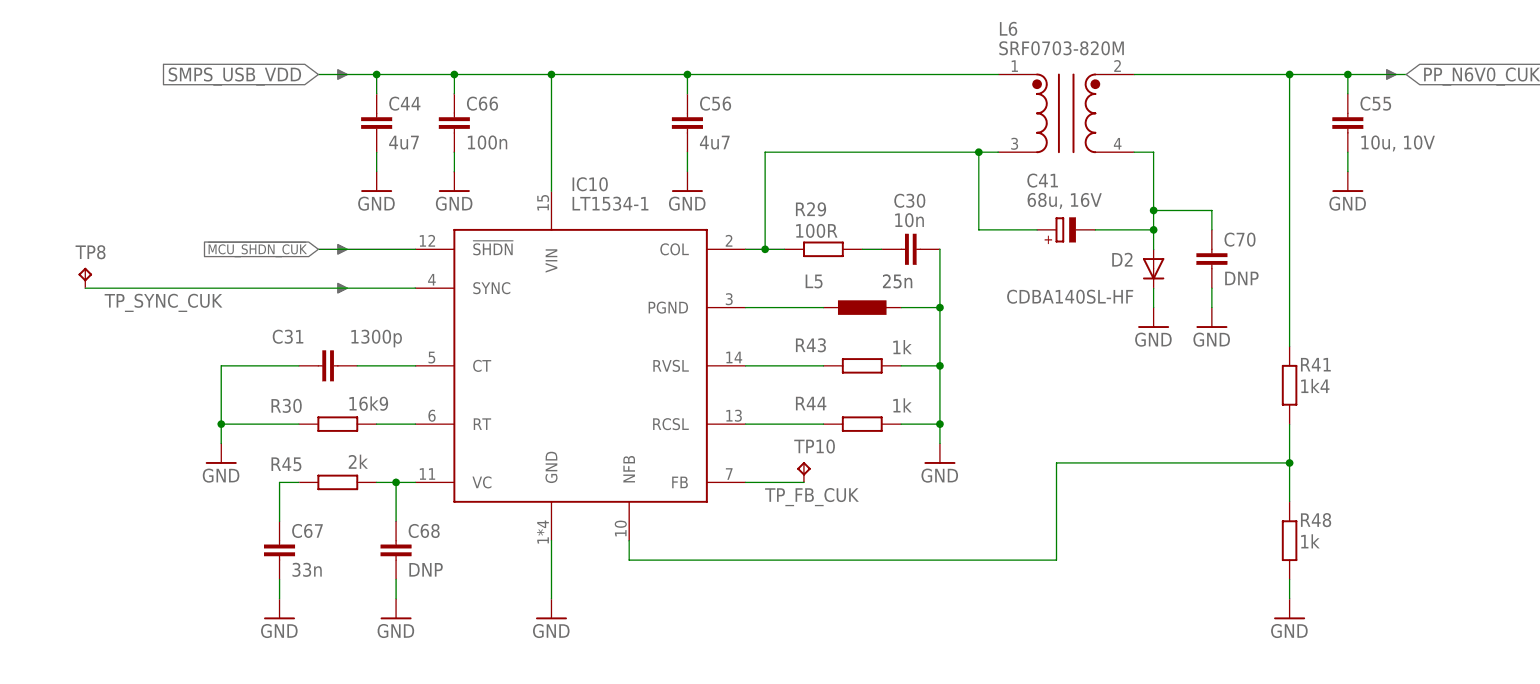
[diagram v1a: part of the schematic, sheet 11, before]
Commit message: Fixed silkscreen errors
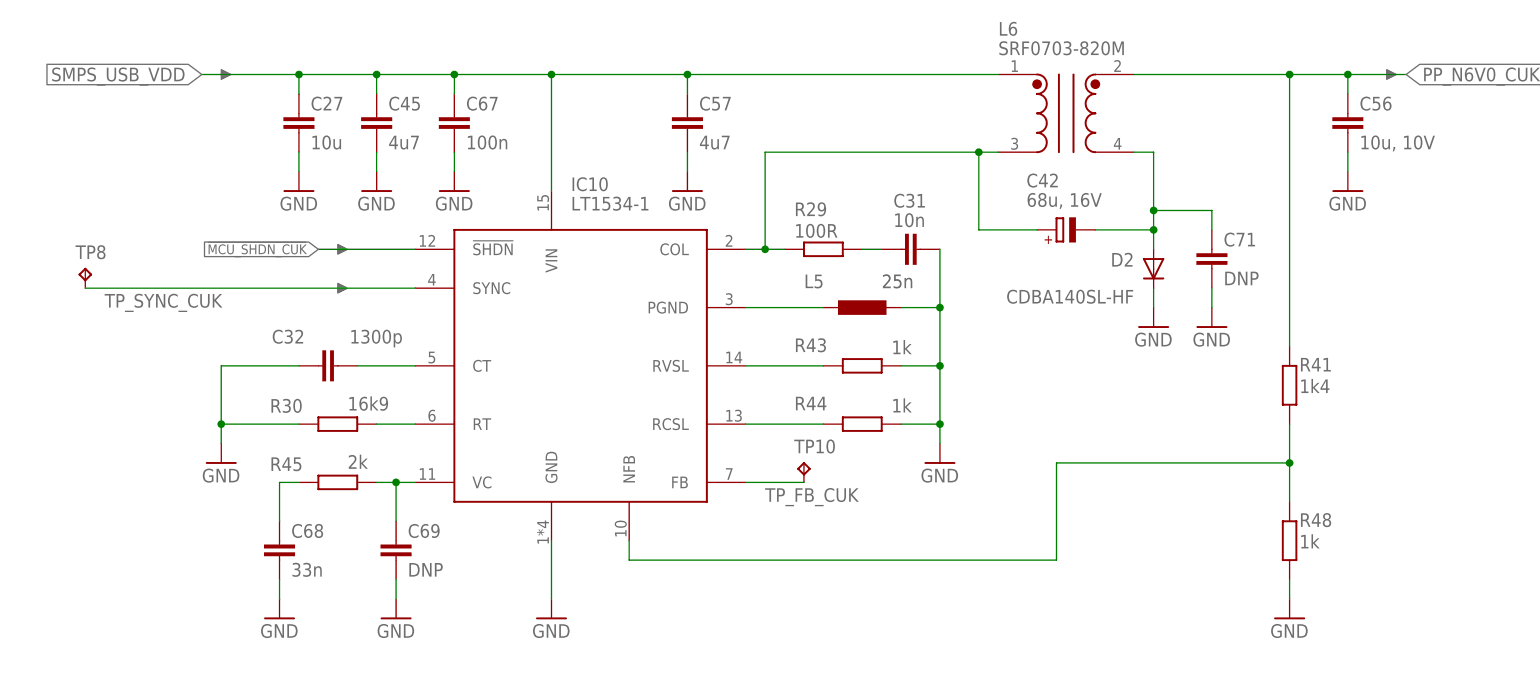
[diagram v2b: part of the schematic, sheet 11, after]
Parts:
- added C113: 100n, rcl:C-EUC0603
- C100: value 47p -> 100n; device rcl:C-EUC0402 -> rcl:C-EUC0603
- C101: value 100n -> 47p; device rcl:C-EUC0603 -> rcl:C-EUC0402
- C102, C107: value 4u7 -> 100n
- C103, C108, C87: value 100n -> 4u7; device rcl-modified-footprints:C-EUC0603 -> rcl:C-EUC0603
- C104: value 10n -> 100n; device rcl:C-EUC0603 -> rcl-modified-footprints:C-EUC0603
- C105, C28, C34, C48, C52, C60, C75: value 100n -> 10n
- C109, C99: device rcl:C-EUC0603 -> rcl-modified-footprints:C-EUC0603
- C27: value 10n -> 10u; device rcl-modified-footprints:C-EUC0402 -> rcl:C-EUC1206
- C29, C33, C37, C43, C49, C53, C65, C73, C77: value 10n -> 100n
- C30, C90: device rcl:C-EUC0603 -> rcl-modified-footprints:C-EUC0402
- C31: value 1300p -> 10n
- C32: value 100n -> 1300p; device rcl-modified-footprints:C-EUC0402 -> rcl:C-EUC0603
- C38: value 10u -> 10n; device rcl:C-EUC0805 -> rcl-modified-footprints:C-EUC0402
- C39: value 10n -> 10u; device rcl-modified-footprints:C-EUC0402 -> rcl:C-EUC0805
- C40, C93: device rcl-modified-footprints:C-EUC0603 -> rcl-modified-footprints:C-EUC0402
- C41: value 68u, 16V -> 10n; device rcl:CPOL-EUCT7343 -> rcl-modified-footprints:C-EUC0603
- C42: value 100n -> 68u, 16V; device rcl-modified-footprints:C-EUC0402 -> rcl:CPOL-EUCT7343
- C44: value 4u7 -> 10n; device rcl:C-EUC0805 -> rcl-modified-footprints:C-EUC0402
- C45: value 100n -> 4u7; device rcl-modified-footprints:C-EUC0603 -> rcl:C-EUC0805
- C46: value 10n -> 100n; device rcl-modified-footprints:C-EUC0402 -> rcl-modified-footprints:C-EUC0603
- C50: value 100p -> 10n
- C51: value 10n -> 100p; device rcl-modified-footprints:C-EUC0603 -> rcl-modified-footprints:C-EUC0402
- C54: value 100n -> 10n; device rcl-modified-footprints:C-EUC0402 -> rcl-modified-footprints:C-EUC0603
- C55: value 10u, 10V -> 100n; device rcl:C-EUC0805 -> rcl-modified-footprints:C-EUC0402
- C56: value 4u7 -> 10u, 10V
- C57: value 100n -> 4u7; device rcl-modified-footprints:C-EUC0402 -> rcl:C-EUC0805
- C59, C80: value 10n -> 100n; device rcl:C-EUC0402 -> rcl-modified-footprints:C-EUC0402
- C61, C83: value 10n -> 100n; device rcl-modified-footprints:C-EUC0402 -> rcl:C-EUC0402
- C64: value 100n -> 10n; device rcl:C-EUC0402 -> rcl-modified-footprints:C-EUC0402
- C66: value 100n -> 10n; device rcl:C-EUC0603 -> rcl:C-EUC0402
- C67: value 33n -> 100n
- C68: value DNP -> 33n
- C69: value 100p -> DNP; device rcl-modified-footprints:C-EUC0603 -> rcl:C-EUC0603
- C70: value DNP -> 100p; device rcl:C-EUC0603 -> rcl-modified-footprints:C-EUC0603
- C71, C79, C92: device rcl-modified-footprints:C-EUC0402 -> rcl:C-EUC0603
- C72: value 100n -> DNP; device rcl:C-EUC0402 -> rcl-modified-footprints:C-EUC0402
- C74, C95: device rcl-modified-footprints:C-EUC0603 -> rcl:C-EUC0402
- C76, C88: device rcl-modified-footprints:C-EUC0402 -> rcl-modified-footprints:C-EUC0603
- C78: value 100n -> 10n; device rcl:C-EUC0603 -> rcl-modified-footprints:C-EUC0402
- C81: device rcl:C-EUC0603 -> rcl:C-EUC0402
- C82: value 100n -> 10n; device rcl:C-EUC0402 -> rcl:C-EUC0603
- C85: value 4u7 -> 10n; device rcl:C-EUC0603 -> rcl-modified-footprints:C-EUC0402
- C94: device rcl:C-EUC0402 -> rcl-modified-footprints:C-EUC0603
- C96: value 10n -> 100n; device rcl:C-EUC0402 -> rcl-modified-footprints:C-EUC0603
- C97: value 47p -> 10n
- C98: value 100n -> 47p; device rcl-modified-footprints:C-EUC0603 -> rcl:C-EUC0402
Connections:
- net DIAMOND_IBIAS_BOTTOM: now also C52.2; no longer C51.2
- net DIAMOND_IBIAS_TOP: now also C52.1; no longer C51.1
- net DMD_OP_NPN: now also C51.1; no longer C50.1
- net DMD_OP_PNP: now also C51.2; no longer C50.2
- net GND: now also C113.2, C40.2, C50.2, C71.2, C78.2; no longer C42.2, C52.2, C72.2, C79.2
- net LDO_N10V0_FB_CH1: now also C41.2; no longer C40.2
- net LDO_N10V0_NR_SS_CH1: now also C54.1; no longer C53.1
- net MCU_NRST: now also C82.1; no longer C81.1
- net MCU_PB11: now also C104.1; no longer C103.1
- net MCU_USB_FS_D_N: now also C101.1; no longer C100.1
- net MCU_USB_FS_D_P: now also C98.1; no longer C97.1
- net MCU_VCAP_2: now also C112.1; no longer C111.1
- net N$11: now also C72.2; no longer C71.2
- net N$12: now also C79.1; no longer C78.1
- net N$13: now also C72.1; no longer C71.1
- net N$62: now also C31.1; no longer C30.1
- net N$63: now also C68.1; no longer C67.1
- net N$64: now also C69.1; no longer C68.1
- net N$68: now also C42.+; no longer C41.+
- net N$69: now also C42.-, C71.1; no longer C41.-, C70.1
- net N$8: now also C32.1; no longer C31.1
- net ONE_SHOT_CAP: now also C70.1; no longer C69.1
- net PP_N5V0_ANALOG: now also C39.1, C41.1, C46.1, C55.1, C62.1, C80.1, C94.1; no longer C36.1, C40.1, C45.1, C54.1, C61.1, C79.1, C93.1
- net PP_N6V0_CUK: now also C53.1, C56.1; no longer C52.1, C55.1
- net PP_P15V0_ANALOG: now also C76.1; no longer C74.1
- net PP_P3V3: now also C106.1, C111.1, C28.1, C35.1, C44.1, C49.1, C61.1, C66.1, C74.1, C81.1, C85.1, C87.1, C91.1, C97.1, C99.1; no longer C105.1, C108.1, C27.1, C34.1, C42.1, C47.1, C57.1, C62.1, C72.1, C80.1, C82.1, C86.1, C88.1, C94.1, C98.1
- net PP_P3V3_VDDA: now also C86.1, C92.1; no longer C85.1, C91.1
- net PP_P5V0_ANALOG: now also C100.1, C30.1, C36.1, C40.1, C47.1, C50.1, C78.1, C88.1, C93.1; no longer C28.1, C35.1, C39.1, C46.1, C49.1, C76.1, C87.1, C92.1, C99.1
- net PP_P5V0_DAC1: now also C103.1; no longer C101.1
- net SMPS_USB_VDD: now also C113.1, C27.1, C45.1, C57.1, C67.1, C79.2; no longer C112.1, C44.1, C56.1, C66.1, C78.2
- net USBCONN_P1: now also C105.1; no longer C104.1
- net USB_VDD: now also C108.1; no longer C106.1
- net VREF_AV_DET: now also C34.1; no longer C32.1
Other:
- moved on the sheet: C102, C105, C106, C107, C111, C29, C31, C33, C34, C35, C36, C37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

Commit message: Added renaming script and started
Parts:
- C23, C29, C33, C35, C36, C37, C43, C49, C55, C58, C59, C61, C65, C73, C77, C80, C83, C89, C90, C93, C95: value 100n -> CAP CER 0.1UF 10V X7R 0402 10%
